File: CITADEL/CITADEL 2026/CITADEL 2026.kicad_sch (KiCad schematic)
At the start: 58 parts, among them J1 Vibration Motor, J10 Faerie CAN BUS, J11 Servo_Daughter, J18 CAN BUS, J19 Battery Connections, J2 Stepper 1, J3 LED Strip, J4 Spark Max PWM, J5 Spark Max PWR, J6 Faerie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

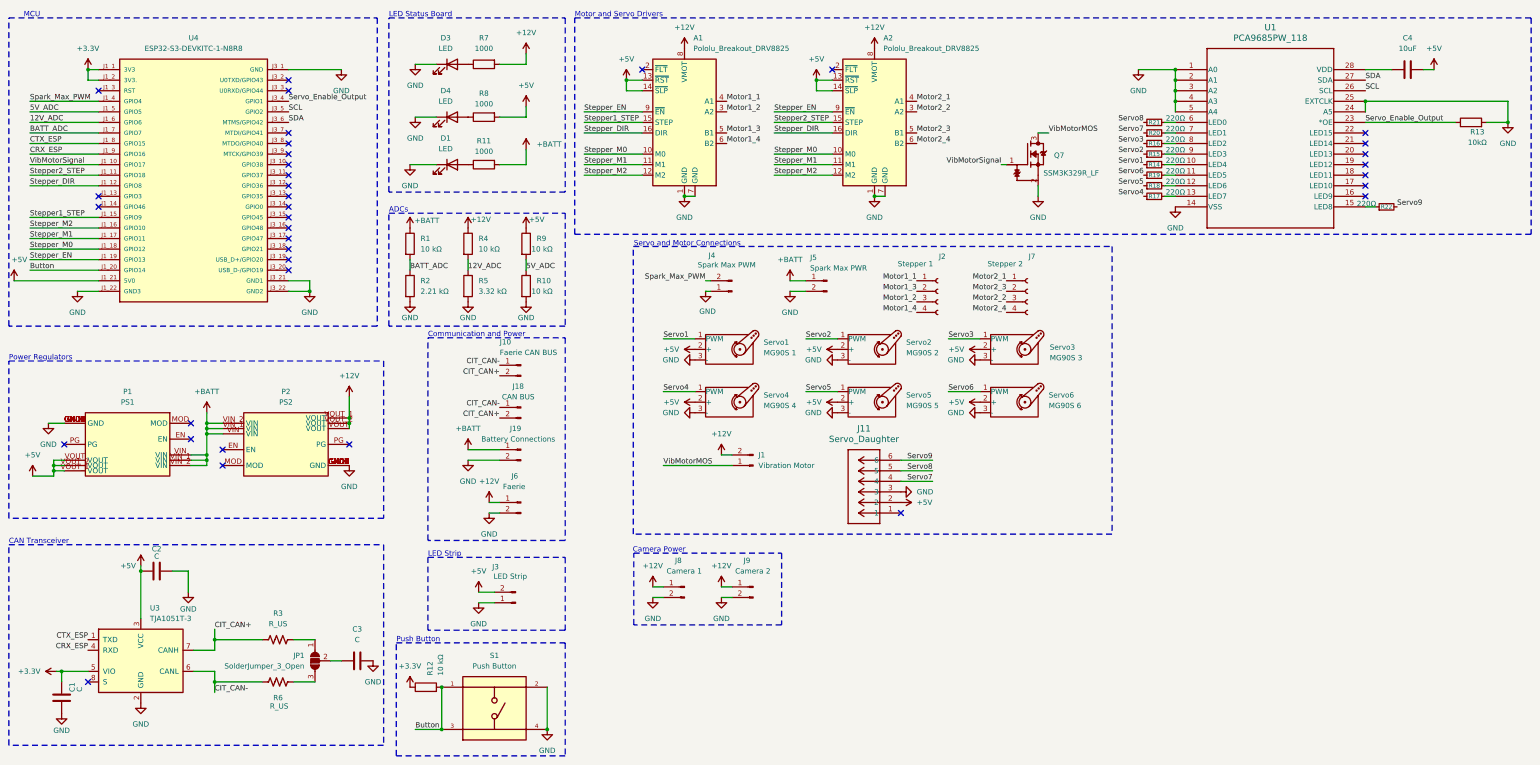
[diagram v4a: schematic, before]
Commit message: Updated servo connectors and ESC comms
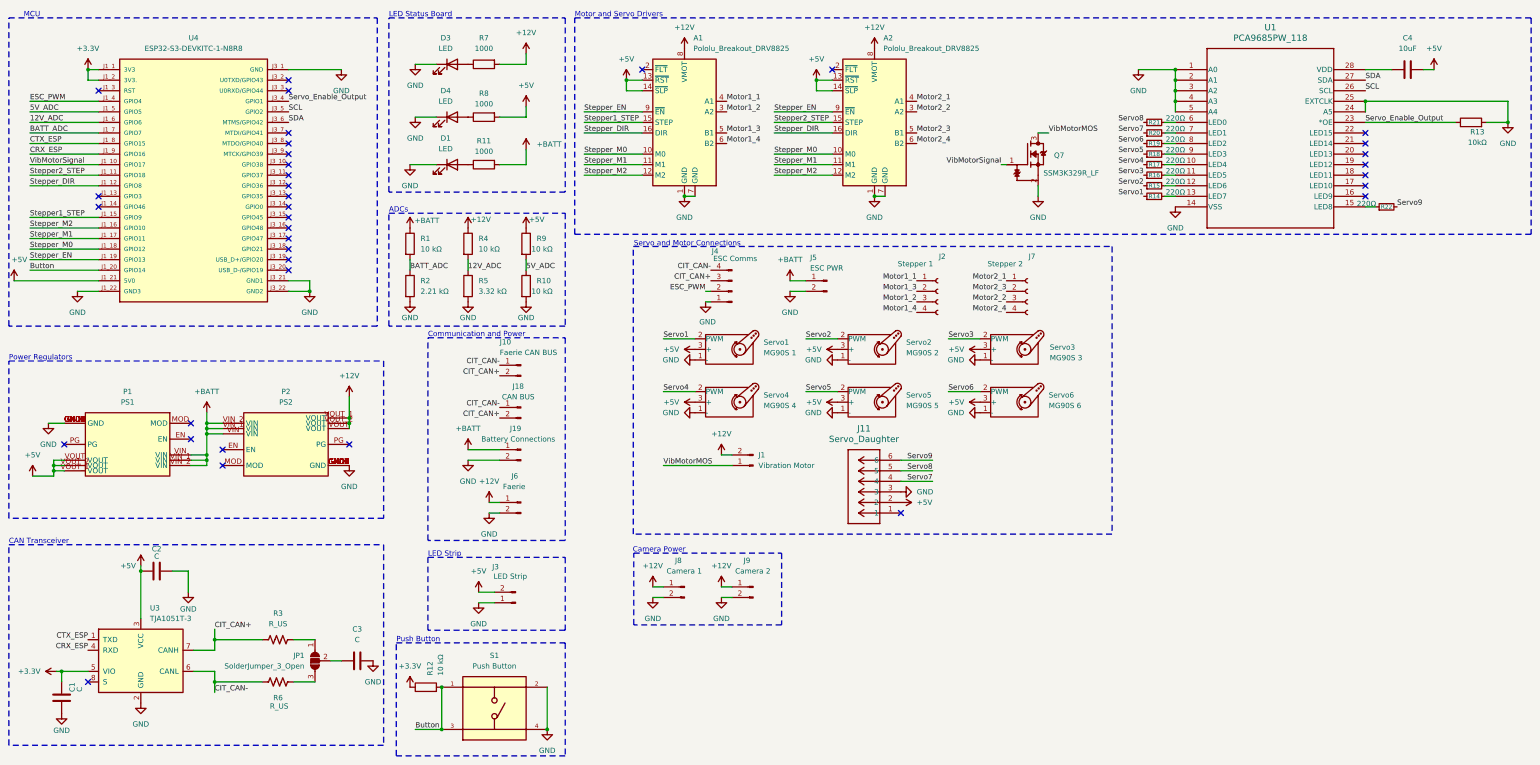
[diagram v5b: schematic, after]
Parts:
- J4: value Spark Max PWM -> ESC Comms; footprint Connector_PinHeader_2.54mm:PinHeader_1x02_P2.54mm_Vertical -> Connector_PinHeader_2.54mm:PinHeader_1x04_P2.54mm_Vertical; symbol Connector:Conn_01x02_Pin -> Connector:Conn_01x04_Pin
- J5: value Spark Max PWR -> ESC PWR
- Servo1, Servo2, Servo3, Servo4, Servo5, Servo6: footprint Connector_PinHeader_2.54mm:PinHeader_1x03_P2.54mm_Vertical -> Connector_Molex:Molex_Mini-Fit_Jr_5566-04A_2x02_P4.20mm_Vertical
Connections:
- net +5V: now also Servo1.3 (+), Servo2.3 (+), Servo3.3 (+), Servo4.3 (+), Servo5.3 (+), Servo6.3 (+); no longer Servo1.2 (+), Servo2.2 (+), Servo3.2 (+), Servo4.2 (+), Servo5.2 (+), Servo6.2 (+)
- net CIT_CAN+: now also J4.3 (Pin_3)
- net CIT_CAN-: now also J4.4 (Pin_4)
- net GND: now also Servo1.1 (-), Servo2.1 (-), Servo3.1 (-), Servo4.1 (-), Servo5.1 (-), Servo6.1 (-); no longer Servo1.3 (-), Servo2.3 (-), Servo3.3 (-), Servo4.3 (-), Servo5.3 (-), Servo6.3 (-)
- net Servo1: now also Servo1.2 (PWM); no longer Servo1.1 (PWM)
- net Servo2: now also Servo2.2 (PWM); no longer Servo2.1 (PWM)
- net Servo3: now also Servo3.2 (PWM); no longer Servo3.1 (PWM)
- net Servo4: now also Servo4.2 (PWM); no longer Servo4.1 (PWM)
- net Servo5: now also Servo5.2 (PWM); no longer Servo5.1 (PWM)
- net Servo6: now also Servo6.2 (PWM); no longer Servo6.1 (PWM)
- net at R14.2: now also U1.13 (LED7); no longer U1.10 (LED4)
- net at R19.2: now also U1.8 (LED2); no longer U1.11 (LED5)
- net at R16.2: now also U1.11 (LED5); no longer U1.8 (LED2)
- net at R18.2: now also U1.9 (LED3); no longer U1.12 (LED6)
- net at R15.2: now also U1.12 (LED6); no longer U1.9 (LED3)
- net at R17.2: now also U1.10 (LED4); no longer U1.13 (LED7)
- net Spark_Max_PWM renamed ESC_PWM
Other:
- moved on the sheet: R14, R15, R16, R17, R18, R19

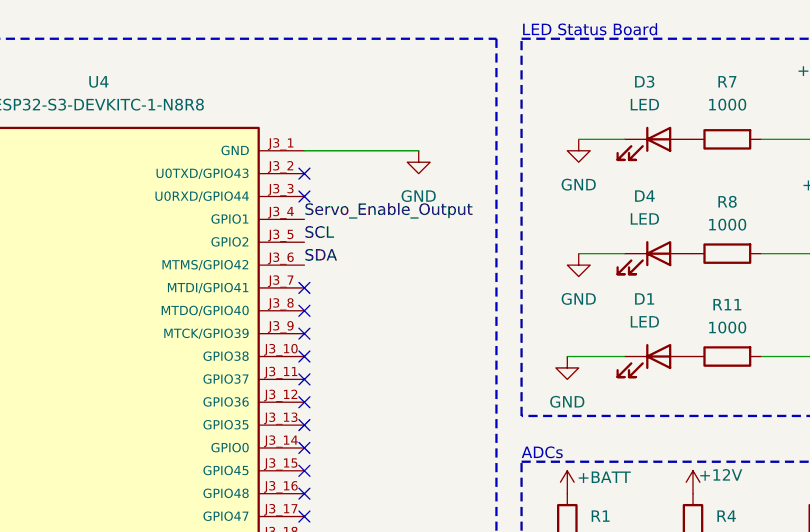
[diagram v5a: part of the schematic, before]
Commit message: Added I²C pullups
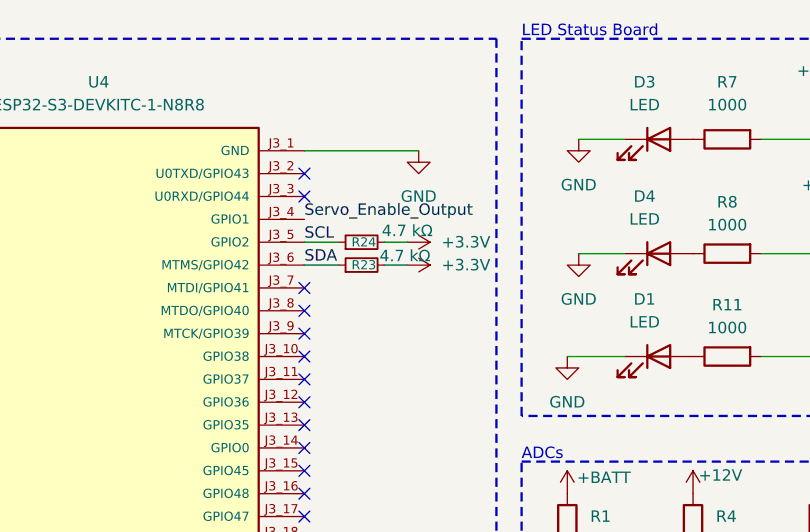
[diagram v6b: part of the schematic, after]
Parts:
- added R23, R24: 4.7 kΩ, Resistor_SMD:R_0603_1608Metric_Pad0.98x0.95mm_HandSolder, symbol Device:R_Small
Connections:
- net +3.3V: now also R23.2, R24.2
- net SCL: now also R24.1
- net SDA: now also R23.1
